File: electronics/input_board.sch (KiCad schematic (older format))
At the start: 16 parts, among them P1 CONN_01X02, Q1 IRLZ44N, Q2 IRF9Z34, Q3 IRLZ44N, Q4 IRLZ44N

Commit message: migrated to 0805 for passives
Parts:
- C3: footprint Capacitors_SMD:C_0603_HandSoldering -> Capacitors_SMD:C_0805_HandSoldering
- R2, R3, R4: footprint Resistors_SMD:R_0603_HandSoldering -> Resistors_SMD:R_0805_HandSoldering
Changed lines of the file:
@@
 F 0 "C3" H 5400 2150 50  0000 L CNN
 F 1 "100n" H 5400 1950 50  0000 L CNN
-F 2 "Capacitors_SMD:C_0603_HandSoldering" H 5388 1900 30  0001 C CNN
+F 2 "Capacitors_SMD:C_0805_HandSoldering" H 5388 1900 30  0001 C CNN
 F 3 "" H 5350 2050 60  0000 C CNN
 	1    5350 2050
@@
 F 0 "R2" H 5850 2200 50  0000 C CNN
 F 1 "1k" V 5757 2401 50  0000 C CNN
-F 2 "Resistors_SMD:R_0603_HandSoldering" V 5680 2400 30  0001 C CNN
+F 2 "Resistors_SMD:R_0805_HandSoldering" V 5680 2400 30  0001 C CNN
 F 3 "" H 5750 2400 30  0000 C CNN
 	1    5750 2400
@@
 F 0 "R3" H 9150 2150 50  0000 C CNN
 F 1 "10k" V 9057 2251 50  0000 C CNN
-F 2 "Resistors_SMD:R_0603_HandSoldering" V 8980 2250 30  0001 C CNN
+F 2 "Resistors_SMD:R_0805_HandSoldering" V 8980 2250 30  0001 C CNN
 F 3 "" H 9050 2250 30  0000 C CNN
 	1    9050 2250
@@
 F 0 "R4" V 9200 1900 50  0000 C CNN
 F 1 "1k" V 9307 1901 50  0000 C CNN
-F 2 "Resistors_SMD:R_0603_HandSoldering" V 9230 1900 30  0001 C CNN
+F 2 "Resistors_SMD:R_0805_HandSoldering" V 9230 1900 30  0001 C CNN
 F 3 "" H 9300 1900 30  0000 C CNN
 	1    9300 1900

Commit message: assigning actual footprints to the input board
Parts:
- removed P1: CONN_01X02, Terminal_Blocks:TerminalBlock_WAGO-236_2Stift_RM5mm_2pol, symbol CONN_01X02
- removed Q1: IRLZ44N, symbol Q_NMOS_GDS
- removed Q2: IRF9Z34, symbol Q_PMOS_GDS
- added U1: BSL316C, TSOP6, symbol BSL316C
- C2: renamed from C4; footprint Capacitors_SMD:C_0603_HandSoldering -> Capacitors_SMD:C_0805_HandSoldering
- renumbered C3 to C1, C5 to C3, C6 to C4, D2 to D1, D3 to D2, Q3 to Q1, Q4 to Q2
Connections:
- wire segments 44 -> 43
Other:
- note added: "Inverter"
- note removed: "Low power MOSFETs"
- moved on the sheet: C1, C2, C3, C4, D1, D2, F1, Q1, Q2, R1, R2, R3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

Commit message: all passives to 1206
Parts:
- C1: footprint Capacitors_SMD:C_0805_HandSoldering -> Capacitors_SMD:C_1206_HandSoldering
- C3, C4: footprint Capacitors_SMD:C_0603_HandSoldering -> Capacitors_SMD:C_1206_HandSoldering
- R2, R3, R4: footprint Resistors_SMD:R_0805_HandSoldering -> Resistors_SMD:R_1206_HandSoldering
- U1: footprint TSOP6 -> TO SOT SMD:TSOT-6-MK06A_Handsoldering
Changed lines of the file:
@@
 F 0 "C1" H 4550 2150 50  0000 L CNN
 F 1 "100n" H 4550 1950 50  0000 L CNN
-F 2 "Capacitors_SMD:C_0805_HandSoldering" H 4538 1900 30  0001 C CNN
+F 2 "Capacitors_SMD:C_1206_HandSoldering" H 4538 1900 30  0001 C CNN
 F 3 "" H 4500 2050 60  0000 C CNN
 	1    4500 2050
@@
 F 0 "R2" H 5000 2200 50  0000 C CNN
 F 1 "1k" V 4907 2401 50  0000 C CNN
-F 2 "Resistors_SMD:R_0805_HandSoldering" V 4830 2400 30  0001 C CNN
+F 2 "Resistors_SMD:R_1206_HandSoldering" V 4830 2400 30  0001 C CNN
 F 3 "" H 4900 2400 30  0000 C CNN
 	1    4900 2400
@@
 F 0 "R3" H 8875 2150 50  0000 C CNN
 F 1 "10k" V 8782 2251 50  0000 C CNN
-F 2 "Resistors_SMD:R_0805_HandSoldering" V 8705 2250 30  0001 C CNN
+F 2 "Resistors_SMD:R_1206_HandSoldering" V 8705 2250 30  0001 C CNN
 F 3 "" H 8775 2250 30  0000 C CNN
 	1    8775 2250
@@
 F 0 "R4" V 8925 1900 50  0000 C CNN
 F 1 "1k" V 9032 1901 50  0000 C CNN
-F 2 "Resistors_SMD:R_0805_HandSoldering" V 8955 1900 30  0001 C CNN
+F 2 "Resistors_SMD:R_1206_HandSoldering" V 8955 1900 30  0001 C CNN
 F 3 "" H 9025 1900 30  0000 C CNN
 	1    9025 1900
@@
 F 0 "C4" H 9275 2350 50  0000 L CNN
 F 1 "10u" H 9275 2150 50  0000 L CNN
-F 2 "Capacitors_SMD:C_0603_HandSoldering" H 9263 2100 30  0001 C CNN
+F 2 "Capacitors_SMD:C_1206_HandSoldering" H 9263 2100 30  0001 C CNN
 F 3 "" H 9225 2250 60  0000 C CNN
 	1    9225 2250
@@
 F 0 "C3" H 7675 2350 50  0000 L CNN
 F 1 "47n" H 7675 2150 50  0000 L CNN
-F 2 "Capacitors_SMD:C_0603_HandSoldering" H 7663 2100 30  0001 C CNN
+F 2 "Capacitors_SMD:C_1206_HandSoldering" H 7663 2100 30  0001 C CNN
 F 3 "" H 7625 2250 60  0000 C CNN
 	1    7625 2250
@@
 F 0 "U1" V 5725 2250 50  0000 L CNN
 F 1 "BSL316C" V 6425 1925 50  0000 L CNN
-F 2 "TSOP6" V 6400 2375 50  0001 L CIN
+F 2 "TO SOT SMD:TSOT-6-MK06A_Handsoldering" V 6400 2375 50  0001 L CIN
 F 3 "" H 5875 2175 50  0000 L CNN
 	1    6075 2000

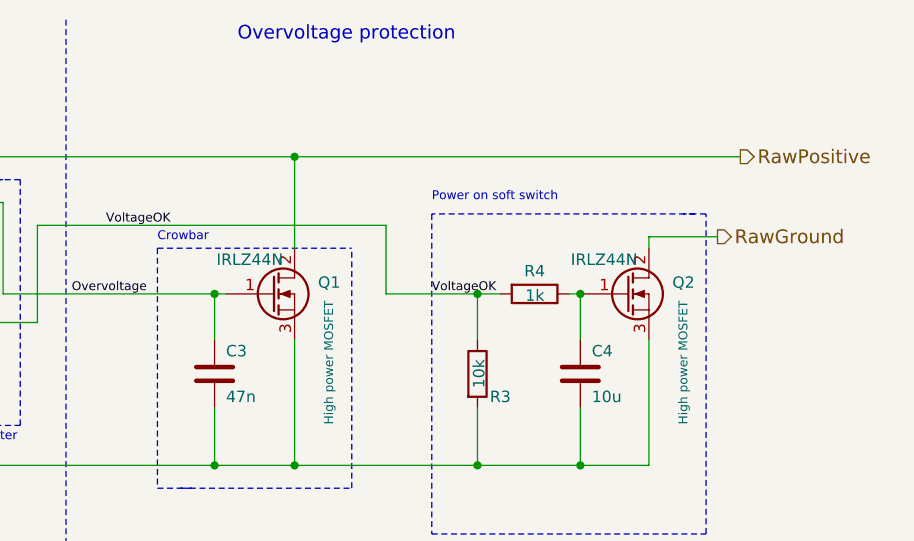
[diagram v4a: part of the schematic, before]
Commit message: changed power mosfets to IRFR13N20D
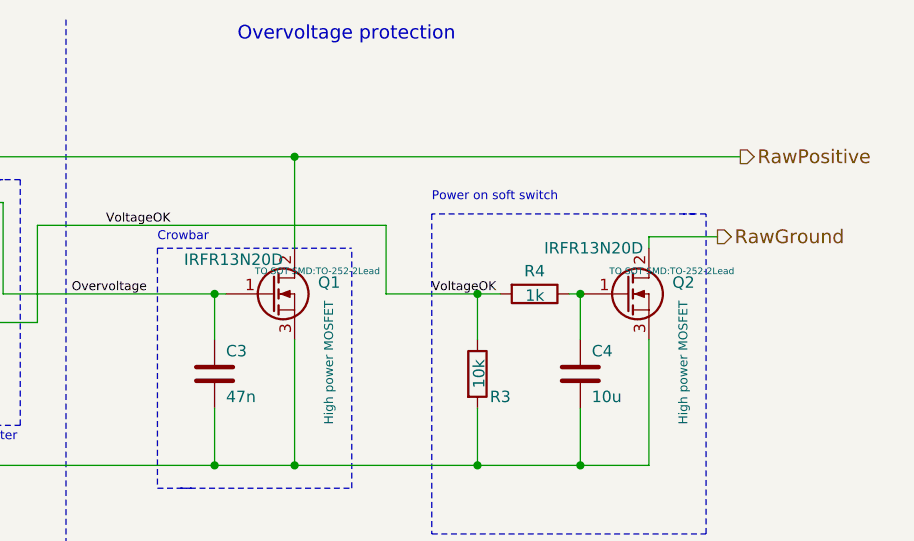
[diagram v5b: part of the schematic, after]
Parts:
- Q1, Q2: value IRLZ44N -> IRFR13N20D; footprint (none) -> TO SOT SMD:TO-252-2Lead
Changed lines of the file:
@@
 $Descr A4 11693 8268
 encoding utf-8
-Sheet 3 2
+Sheet 2 2
 Title "Sunpowered Input Board"
 Date ""
@@
 P 9425 1900
 F 0 "Q2" H 9725 1950 50  0000 R CNN
-F 1 "IRLZ44N" H 9475 2050 50  0000 R CNN
-F 2 "" H 9625 2000 29  0000 C CNN
+F 1 "IRFR13N20D" H 9500 2100 50  0000 R CNN
+F 2 "TO SOT SMD:TO-252-2Lead" H 9625 2000 29  0000 C CNN
 F 3 "" H 9425 1900 60  0000 C CNN
 F 4 "High power MOSFET" V 9675 1600 39  0000 C CNN "Note"
@@
 P 7875 1900
 F 0 "Q1" H 8175 1950 50  0000 R CNN
-F 1 "IRLZ44N" H 7925 2050 50  0000 R CNN
-F 2 "" H 8075 2000 29  0000 C CNN
+F 1 "IRFR13N20D" H 7925 2050 50  0000 R CNN
+F 2 "TO SOT SMD:TO-252-2Lead" H 8075 2000 29  0000 C CNN
 F 3 "" H 7875 1900 60  0000 C CNN
 F 4 "High power MOSFET" V 8125 1600 39  0000 C CNN "Note"

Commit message: corrected footprints for diodes
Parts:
- D1: footprint Diodes_SMD:D-Pak_TO252AA -> Diodes SMD:D-Pak_TO252AA
- D2: footprint Diodes_SMD:Diode-SMB_Standard -> Diodes SMD:SMB_Standard
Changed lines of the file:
@@
 F 0 "D2" V 4900 1850 50  0000 C CNN
 F 1 "22V" V 4800 1850 50  0000 C CNN
-F 2 "Diodes_SMD:Diode-SMB_Standard" H 4900 1750 60  0001 C CNN
+F 2 "Diodes SMD:SMB_Standard" H 4900 1750 60  0001 C CNN
 F 3 "http://www.tme.eu/pl/Document/c2d23b0bf5a10da03f2379b0c2e473b6/1SMB5913BT3-D.PDF" H 4900 1750 60  0001 C CNN
 	1    4900 1750
@@
 F 0 "D1" H 4150 1400 50  0000 C CNN
 F 1 "12A" H 4150 1200 50  0000 C CNN
-F 2 "Diodes_SMD:D-Pak_TO252AA" H 4150 1300 60  0001 C CNN
+F 2 "Diodes SMD:D-Pak_TO252AA" H 4150 1300 60  0001 C CNN
 F 3 "http://www.vishay.com/docs/89094/v12p12.pdf" H 4150 1300 60  0001 C CNN
 	1    4150 1300

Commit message: overvoltage detector layout
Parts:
- removed D1: 12A, Diodes SMD:D-Pak_TO252AA, symbol D_Schottky
- added D1: 12A, TO SOT SMD:TO-252-2Lead, symbol SCHDPAK
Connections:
- net PowerIn+ is gone; now on net PanelVoltageSense+: F1.1
- net PanelVoltageSense+: now also D1.1 (A), D1.3 (A)
- net RawPositive: now also D1.2 (K)
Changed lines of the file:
@@
 Power on soft switch
-$Comp
-L D_Schottky D1
-U 1 1 55EBE3EF
-P 4150 1300
-F 0 "D1" H 4150 1400 50  0000 C CNN
-F 1 "12A" H 4150 1200 50  0000 C CNN
-F 2 "Diodes SMD:D-Pak_TO252AA" H 4150 1300 60  0001 C CNN
-F 3 "http://www.vishay.com/docs/89094/v12p12.pdf" H 4150 1300 60  0001 C CNN
-	1    4150 1300
-	-1   0    0    1
-$EndComp
 $Comp
 L C C4
@@
 	9525 1650 9825 1650
 Wire Wire Line
-	2550 1300 4000 1300
+	2550 1300 4100 1300
 Wire Wire Line
 	2950 1050 2950 1300
@@
 	8375 1900 8875 1900
 Wire Wire Line
-	7975 1300 7975 1700
+	7975 1275 7975 1700
 Wire Wire Line
 	7975 2100 7975 2650
@@
 	6525 1900 6525 2200
 Wire Wire Line
-	5850 1900 5850 1300
+	5850 1300 5850 1900
 Connection ~ 5850 1300
 Wire Wire Line
@@
 Wire Wire Line
 	5650 2000 5650 1500
-Wire Wire Line
-	4300 1300 9925 1300
 Wire Wire Line
 	8375 1600 6850 1600
@@
 Text Notes 6550 2550 0    39   ~ 0
 Inverter
+$Comp
+L SCHDPAK D1
+U 1 1 567D7FA2
+P 4300 1300
+F 0 "D1" H 4300 1400 50  0000 C CNN
+F 1 "12A" H 4300 1200 50  0000 C CNN
+F 2 "TO SOT SMD:TO-252-2Lead" H 4300 1300 50  0001 C CNN
+F 3 "http://www.vishay.com/docs/89094/v12p12.pdf" H 4300 1300 50  0001 C CNN
+	1    4300 1300
+	-1   0    0    1
+$EndComp
+Wire Wire Line
+	4100 1250 4100 1350
+Connection ~ 4100 1300
+Wire Wire Line
+	4500 1300 9925 1300
+Text Label 3525 1300 0    39   ~ 0
+PowerIn+
+Text Label 4500 1300 0    39   ~ 0
+InputPower
+Text Label 3650 2650 0    39   ~ 0
+InputGround
+Text Label 2600 1300 0    39   ~ 0
+PowerIn+
 $EndSCHEMATC

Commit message: basic layout for the input board
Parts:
- C2: footprint Capacitors_SMD:C_0805_HandSoldering -> Capacitors_SMD:C_1206_HandSoldering
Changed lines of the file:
@@
 F 0 "C2" H 5300 2550 50  0000 L CNN
 F 1 "47n" H 5300 2350 50  0000 L CNN
-F 2 "Capacitors_SMD:C_0805_HandSoldering" H 5288 2300 30  0001 C CNN
+F 2 "Capacitors_SMD:C_1206_HandSoldering" H 5288 2300 30  0001 C CNN
 F 3 "" H 5250 2450 60  0000 C CNN
 	1    5250 2450
